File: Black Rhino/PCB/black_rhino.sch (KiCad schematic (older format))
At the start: 150 parts, among them SW1 SW_Push, U1 ATmega32U4-AU, Y1 16MHz

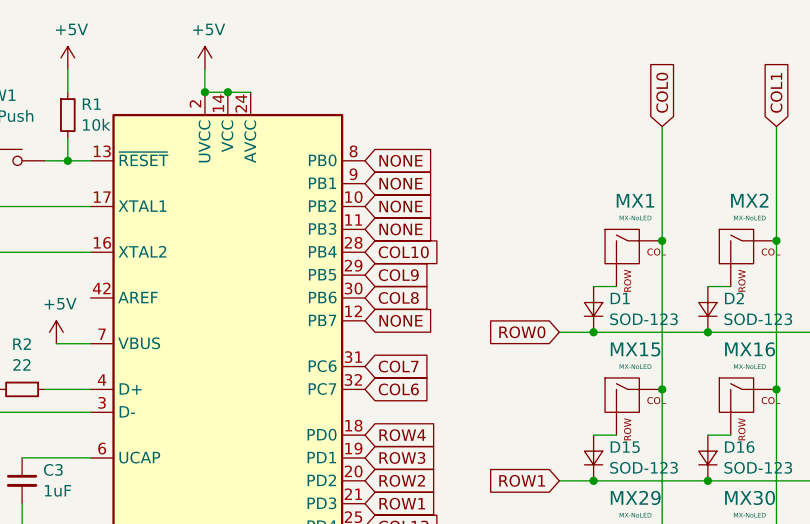
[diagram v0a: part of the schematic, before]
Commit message: Wire Black-Rhino-PCB
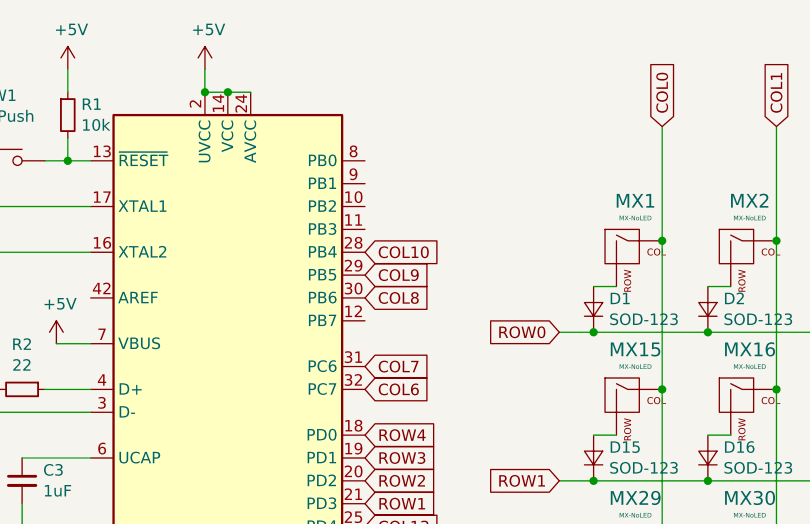
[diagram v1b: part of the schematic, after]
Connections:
- removed net NONE: U1.10 (PB2), U1.11 (PB3), U1.12 (PB7), U1.8 (PB0), U1.9 (PB1)
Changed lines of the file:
@@
 Text GLabel 10950 1000 1    50   Input ~ 0
 COL13
-Text GLabel 3150 1850 2    50   Input ~ 0
-NONE
-Text GLabel 3150 1450 2    50   Input ~ 0
-NONE
-Text GLabel 3150 1350 2    50   Input ~ 0
-NONE
-Text GLabel 3150 1250 2    50   Input ~ 0
-NONE
-Text GLabel 3150 1150 2    50   Input ~ 0
-NONE
 Text GLabel 3150 3550 2    50   Input ~ 0
 COL0

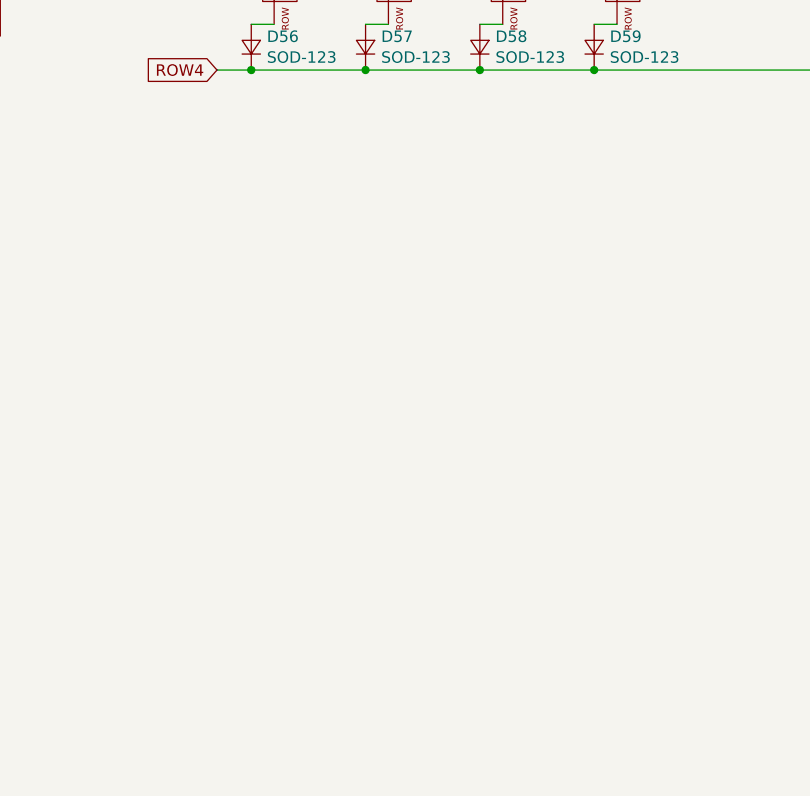
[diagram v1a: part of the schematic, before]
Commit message: Improve Black-Rhino-PCB & Add MountingHoles
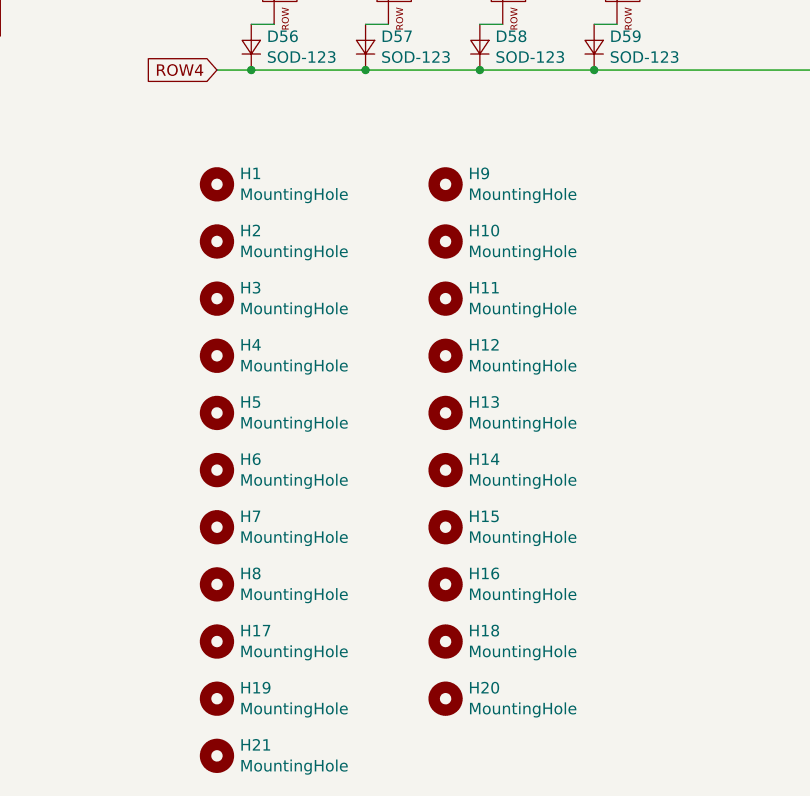
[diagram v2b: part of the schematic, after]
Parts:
- added H1, H10, H11, H12, H13, H14, H15, H16, H17, H18, H19, H2, H20, H21, H3, H4, H5, H6, H7, H8, H9: MountingHole, MountingHole:MountingHole_2mm, symbol Mechanical:MountingHole
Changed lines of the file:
@@
 	8450 4100 8450 3450
 Connection ~ 8450 3450
+$Comp
+L Mechanical:MountingHole H1
+U 1 1 5F254E37
+P 4000 5000
+F 0 "H1" H 4100 5046 50  0000 L CNN
+F 1 "MountingHole" H 4100 4955 50  0000 L CNN
+F 2 "MountingHole:MountingHole_2mm" H 4000 5000 50  0001 C CNN
+F 3 "~" H 4000 5000 50  0001 C CNN
+	1    4000 5000
+	1    0    0    -1
+$EndComp
+$Comp
+L Mechanical:MountingHole H2
+U 1 1 5F256F31
+P 4000 5250
+F 0 "H2" H 4100 5296 50  0000 L CNN
+F 1 "MountingHole" H 4100 5205 50  0000 L CNN
+F 2 "MountingHole:MountingHole_2mm" H 4000 5250 50  0001 C CNN
+F 3 "~" H 4000 5250 50  0001 C CNN
+	1    4000 5250
+	1    0    0    -1
+$EndComp
+$Comp
+L Mechanical:MountingHole H3
+U 1 1 5F26714F
+P 4000 5500
+F 0 "H3" H 4100 5546 50  0000 L CNN
+F 1 "MountingHole" H 4100 5455 50  0000 L CNN
+F 2 "MountingHole:MountingHole_2mm" H 4000 5500 50  0001 C CNN
+F 3 "~" H 4000 5500 50  0001 C CNN
+	1    4000 5500
+	1    0    0    -1
+$EndComp
+$Comp
+L Mechanical:MountingHole H4
+U 1 1 5F277882
+P 4000 5750
+F 0 "H4" H 4100 5796 50  0000 L CNN
+F 1 "MountingHole" H 4100 5705 50  0000 L CNN
+F 2 "MountingHole:MountingHole_2mm" H 4000 5750 50  0001 C CNN
+F 3 "~" H 4000 5750 50  0001 C CNN
+	1    4000 5750
+	1    0    0    -1
+$EndComp
+$Comp
+L Mechanical:MountingHole H5
+U 1 1 5F287B05
+P 4000 6000
+F 0 "H5" H 4100 6046 50  0000 L CNN
+F 1 "MountingHole" H 4100 5955 50  0000 L CNN
+F 2 "MountingHole:MountingHole_2mm" H 4000 6000 50  0001 C CNN
+F 3 "~" H 4000 6000 50  0001 C CNN
+	1    4000 6000
+	1    0    0    -1
+$EndComp
+$Comp
+L Mechanical:MountingHole H6
+U 1 1 5F297D56
+P 4000 6250
+F 0 "H6" H 4100 6296 50  0000 L CNN
+F 1 "MountingHole" H 4100 6205 50  0000 L CNN
+F 2 "MountingHole:MountingHole_2mm" H 4000 6250 50  0001 C CNN
+F 3 "~" H 4000 6250 50  0001 C CNN
+	1    4000 6250
+	1    0    0    -1
+$EndComp
+$Comp
+L Mechanical:MountingHole H7
+U 1 1 5F2A8030
+P 4000 6500
+F 0 "H7" H 4100 6546 50  0000 L CNN
+F 1 "MountingHole" H 4100 6455 50  0000 L CNN
+F 2 "MountingHole:MountingHole_2mm" H 4000 6500 50  0001 C CNN
+F 3 "~" H 4000 6500 50  0001 C CNN
+	1    4000 6500
+	1    0    0    -1
+$EndComp
+$Comp
+L Mechanical:MountingHole H8
+U 1 1 5F2B82E0
+P 4000 6750
+F 0 "H8" H 4100 6796 50  0000 L CNN
+F 1 "MountingHole" H 4100 6705 50  0000 L CNN
+F 2 "MountingHole:MountingHole_2mm" H 4000 6750 50  0001 C CNN
+F 3 "~" H 4000 6750 50  0001 C CNN
+	1    4000 6750
+	1    0    0    -1
+$EndComp
+$Comp
+L Mechanical:MountingHole H9
+U 1 1 5F316618
+P 5000 5000
+F 0 "H9" H 5100 5046 50  0000 L CNN
+F 1 "MountingHole" H 5100 4955 50  0000 L CNN
+F 2 "MountingHole:MountingHole_2mm" H 5000 5000 50  0001 C CNN
+F 3 "~" H 5000 5000 50  0001 C CNN
+	1    5000 5000
+	1    0    0    -1
+$EndComp
+$Comp
+L Mechanical:MountingHole H10
+U 1 1 5F31661E
+P 5000 5250
+F 0 "H10" H 5100 5296 50  0000 L CNN
+F 1 "MountingHole" H 5100 5205 50  0000 L CNN
+F 2 "MountingHole:MountingHole_2mm" H 5000 5250 50  0001 C CNN
+F 3 "~" H 5000 5250 50  0001 C CNN
+	1    5000 5250
+	1    0    0    -1
+$EndComp
+$Comp
+L Mechanical:MountingHole H11
+U 1 1 5F316624
+P 5000 5500
+F 0 "H11" H 5100 5546 50  0000 L CNN
+F 1 "MountingHole" H 5100 5455 50  0000 L CNN
+F 2 "MountingHole:MountingHole_2mm" H 5000 5500 50  0001 C CNN
+F 3 "~" H 5000 5500 50  0001 C CNN
+	1    5000 5500
+	1    0    0    -1
+$EndComp
+$Comp
+L Mechanical:MountingHole H12
+U 1 1 5F31662A
+P 5000 5750
+F 0 "H12" H 5100 5796 50  0000 L CNN
+F 1 "MountingHole" H 5100 5705 50  0000 L CNN
+F 2 "MountingHole:MountingHole_2mm" H 5000 5750 50  0001 C CNN
+F 3 "~" H 5000 5750 50  0001 C CNN
+	1    5000 5750
+	1    0    0    -1
+$EndComp
+$Comp
+L Mechanical:MountingHole H13
+U 1 1 5F316630
+P 5000 6000
+F 0 "H13" H 5100 6046 50  0000 L CNN
+F 1 "MountingHole" H 5100 5955 50  0000 L CNN
+F 2 "MountingHole:MountingHole_2mm" H 5000 6000 50  0001 C CNN
+F 3 "~" H 5000 6000 50  0001 C CNN
+	1    5000 6000
+	1    0    0    -1
+$EndComp
+$Comp
+L Mechanical:MountingHole H14
+U 1 1 5F316636
+P 5000 6250
+F 0 "H14" H 5100 6296 50  0000 L CNN
+F 1 "MountingHole" H 5100 6205 50  0000 L CNN
+F 2 "MountingHole:MountingHole_2mm" H 5000 6250 50  0001 C CNN
+F 3 "~" H 5000 6250 50  0001 C CNN
+	1    5000 6250
+	1    0    0    -1
+$EndComp
+$Comp
+L Mechanical:MountingHole H15
+U 1 1 5F31663C
+P 5000 6500
+F 0 "H15" H 5100 6546 50  0000 L CNN
+F 1 "MountingHole" H 5100 6455 50  0000 L CNN
+F 2 "MountingHole:MountingHole_2mm" H 5000 6500 50  0001 C CNN
+F 3 "~" H 5000 6500 50  0001 C CNN
+	1    5000 6500
+	1    0    0    -1
+$EndComp
+$Comp
+L Mechanical:MountingHole H16
+U 1 1 5F316642
+P 5000 6750
+F 0 "H16" H 5100 6796 50  0000 L CNN
+F 1 "MountingHole" H 5100 6705 50  0000 L CNN
+F 2 "MountingHole:MountingHole_2mm" H 5000 6750 50  0001 C CNN
+F 3 "~" H 5000 6750 50  0001 C CNN
+	1    5000 6750
+	1    0    0    -1
+$EndComp
+$Comp
+L Mechanical:MountingHole H17
+U 1 1 5F34FFBE
+P 4000 7000
+F 0 "H17" H 4100 7046 50  0000 L CNN
+F 1 "MountingHole" H 4100 6955 50  0000 L CNN
+F 2 "MountingHole:MountingHole_2mm" H 4000 7000 50  0001 C CNN
+F 3 "~" H 4000 7000 50  0001 C CNN
+	1    4000 7000
+	1    0    0    -1
+$EndComp
+$Comp
+L Mechanical:MountingHole H18
+U 1 1 5F34FFC4
+P 5000 7000
+F 0 "H18" H 5100 7046 50  0000 L CNN
+F 1 "MountingHole" H 5100 6955 50  0000 L CNN
+F 2 "MountingHole:MountingHole_2mm" H 5000 7000 50  0001 C CNN
+F 3 "~" H 5000 7000 50  0001 C CNN
+	1    5000 7000
+	1    0    0    -1
+$EndComp
+$Comp
+L Mechanical:MountingHole H19
+U 1 1 5F37F0C0
+P 4000 7250
+F 0 "H19" H 4100 7296 50  0000 L CNN
+F 1 "MountingHole" H 4100 7205 50  0000 L CNN
+F 2 "MountingHole:MountingHole_2mm" H 4000 7250 50  0001 C CNN
+F 3 "~" H 4000 7250 50  0001 C CNN
+	1    4000 7250
+	1    0    0    -1
+$EndComp
+$Comp
+L Mechanical:MountingHole H20
+U 1 1 5F37F0C6
+P 5000 7250
+F 0 "H20" H 5100 7296 50  0000 L CNN
+F 1 "MountingHole" H 5100 7205 50  0000 L CNN
+F 2 "MountingHole:MountingHole_2mm" H 5000 7250 50  0001 C CNN
+F 3 "~" H 5000 7250 50  0001 C CNN
+	1    5000 7250
+	1    0    0    -1
+$EndComp
+$Comp
+L Mechanical:MountingHole H21
+U 1 1 5F3B30CA
+P 4000 7500
+F 0 "H21" H 4100 7546 50  0000 L CNN
+F 1 "MountingHole" H 4100 7455 50  0000 L CNN
+F 2 "MountingHole:MountingHole_2mm" H 4000 7500 50  0001 C CNN
+F 3 "~" H 4000 7500 50  0001 C CNN
+	1    4000 7500
+	1    0    0    -1
+$EndComp
 $EndSCHEMATC

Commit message: Fix Black Rhino-PCB & -MountingHoles
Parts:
- added H22: MountingHole, MountingHole:MountingHole_2mm, symbol Mechanical:MountingHole
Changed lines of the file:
@@
+	1    0    0    -1
+$EndComp
+$Comp
+L Mechanical:MountingHole H22
+U 1 1 5F251A42
+P 5000 7500
+F 0 "H22" H 5100 7546 50  0000 L CNN
+F 1 "MountingHole" H 5100 7455 50  0000 L CNN
+F 2 "MountingHole:MountingHole_2mm" H 5000 7500 50  0001 C CNN
+F 3 "~" H 5000 7500 50  0001 C CNN
+	1    5000 7500
 	1    0    0    -1
 $EndComp

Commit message: Add Indicator-LEDs to Black Rhino
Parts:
- added D68, D69, D70: LED, LED_SMD:LED_0805_2012Metric, symbol Device:LED
- added R5, R6, R7: R_Small, Resistor_SMD:R_0805_2012Metric, symbol Device:R_Small
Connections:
- net GND: now also D68.1 (K), D69.1 (K), D70.1 (K)
- net LED1: now reaches U1.10 (PB2)
- net LED1: now also R6.2
- net LED2: now reaches U1.11 (PB3)
- net LED2: now also R7.2
- net LED0: now reaches U1.9 (PB1)
- net LED0: now also R5.2
- new net: D68.2 (A), R5.1
- new net: D69.2 (A), R6.1
- new net: D70.2 (A), R7.1
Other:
- moved on the sheet: C1, C2, C3, C4, C5, C6, C7, D1, D10, D11, D12, D13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

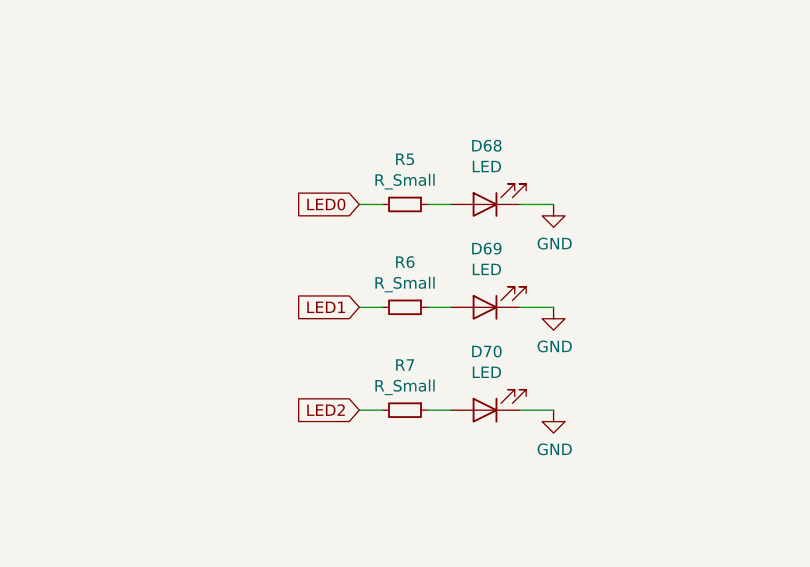
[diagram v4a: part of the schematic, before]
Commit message: Add Ohms to LED-Resistors of Black Rhino
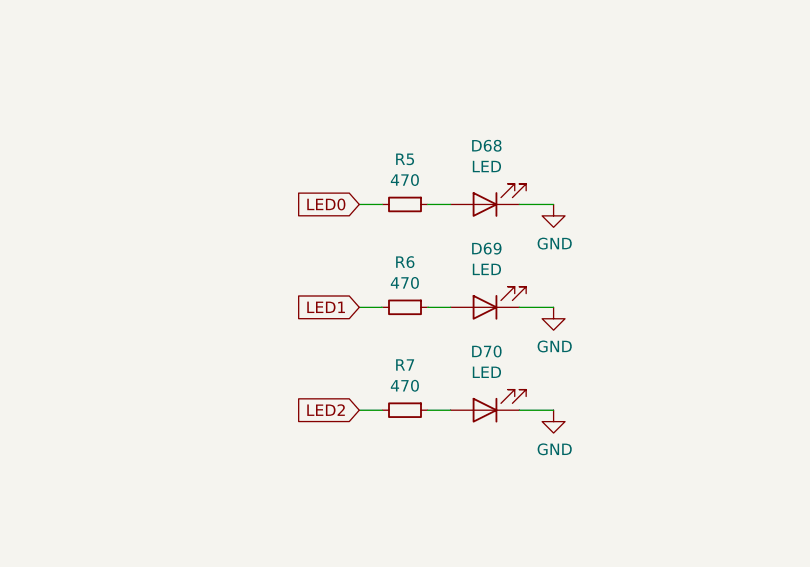
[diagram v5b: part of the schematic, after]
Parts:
- R5, R6, R7: value R_Small -> 470
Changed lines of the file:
@@
-$EndComp
-$Comp
-L Device:R_Small R5
-U 1 1 5F2939FF
-P 3850 6200
-F 0 "R5" V 3654 6200 50  0000 C CNN
-F 1 "R_Small" V 3745 6200 50  0000 C CNN
-F 2 "Resistor_SMD:R_0805_2012Metric" H 3850 6200 50  0001 C CNN
-F 3 "~" H 3850 6200 50  0001 C CNN
-	1    3850 6200
-	0    1    1    0
 $EndComp
 $Comp
@@
 P 3850 6650
 F 0 "R6" V 3654 6650 50  0000 C CNN
-F 1 "R_Small" V 3745 6650 50  0000 C CNN
+F 1 "470" V 3745 6650 50  0000 C CNN
 F 2 "Resistor_SMD:R_0805_2012Metric" H 3850 6650 50  0001 C CNN
 F 3 "~" H 3850 6650 50  0001 C CNN
@@
 P 3850 7100
 F 0 "R7" V 3654 7100 50  0000 C CNN
-F 1 "R_Small" V 3745 7100 50  0000 C CNN
+F 1 "470" V 3745 7100 50  0000 C CNN
 F 2 "Resistor_SMD:R_0805_2012Metric" H 3850 7100 50  0001 C CNN
 F 3 "~" H 3850 7100 50  0001 C CNN
@@
 Wire Wire Line
 	4350 7100 4500 7100
+$Comp
+L Device:R_Small R5
+U 1 1 5F2939FF
+P 3850 6200
+F 0 "R5" V 3654 6200 50  0000 C CNN
+F 1 "470" V 3745 6200 50  0000 C CNN
+F 2 "Resistor_SMD:R_0805_2012Metric" H 3850 6200 50  0001 C CNN
+F 3 "~" H 3850 6200 50  0001 C CNN
+	1    3850 6200
+	0    1    1    0
+$EndComp
 $EndSCHEMATC
